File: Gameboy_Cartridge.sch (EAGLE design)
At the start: 8 parts

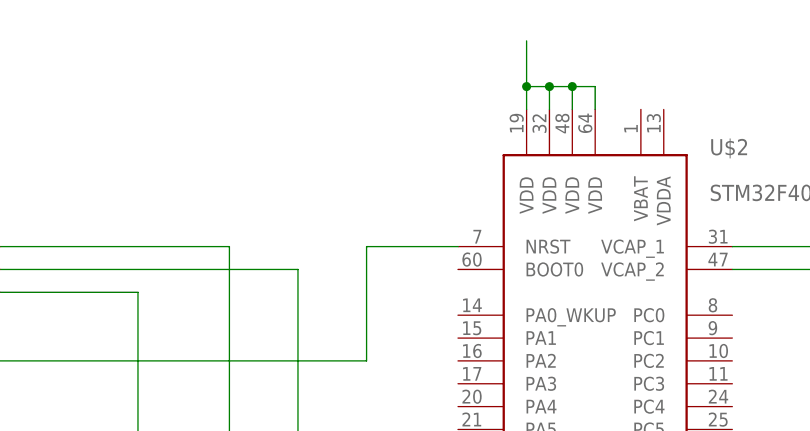
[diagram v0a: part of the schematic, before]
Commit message: BOOT0 10k pullup
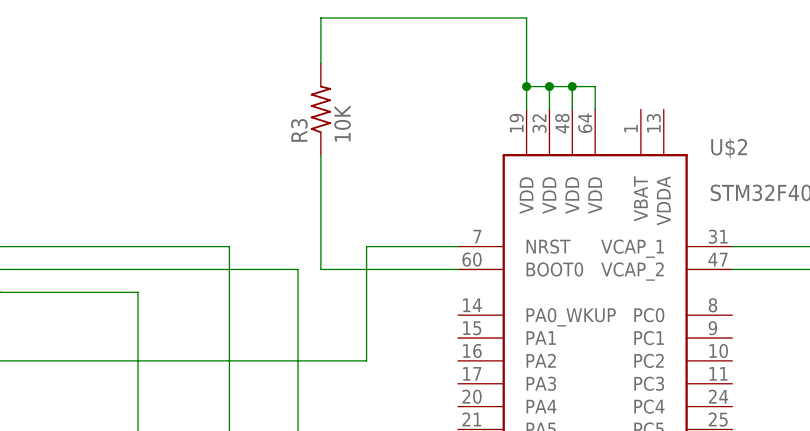
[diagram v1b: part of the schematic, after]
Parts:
- added R3: 10K, resistor:R-US_M0805
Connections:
- new net N$6: R3.1, U$2.BOOT0
- net N$1: now also R3.2
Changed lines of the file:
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@@
 <part name="C2" library="resistor" deviceset="C-EU" device="C0805" value="2.2uF"/>
 <part name="C3" library="resistor" deviceset="C-EU" device="C0805" value="2.2uF"/>
+<part name="R3" library="resistor" deviceset="R-US_" device="M0805" value="10K"/>
 </parts>
 <sheets>
@@
 <instance part="C2" gate="G$1" x="68.58" y="215.9" rot="R90"/>
 <instance part="C3" gate="G$1" x="78.74" y="213.36" rot="R90"/>
+<instance part="R3" gate="G$1" x="2.54" y="231.14" rot="R90"/>
 </instances>
 <busses>
@@
 <wire x1="27.94" y1="231.14" x2="27.94" y2="233.68" width="0.1524" layer="91"/>
 <junction x="27.94" y="233.68"/>
-<wire x1="25.4" y1="233.68" x2="25.4" y2="238.76" width="0.1524" layer="91"/>
+<wire x1="25.4" y1="233.68" x2="25.4" y2="241.3" width="0.1524" layer="91"/>
 <junction x="25.4" y="233.68"/>
+<pinref part="R3" gate="G$1" pin="2"/>
+<wire x1="2.54" y1="236.22" x2="2.54" y2="241.3" width="0.1524" layer="91"/>
+<wire x1="2.54" y1="241.3" x2="25.4" y2="241.3" width="0.1524" layer="91"/>
 </segment>
 </net>
@@
 </segment>
 </net>
+<net name="N$6" class="0">
+<segment>
+<pinref part="U$2" gate="G$1" pin="BOOT0"/>
+<wire x1="17.78" y1="213.36" x2="2.54" y2="213.36" width="0.1524" layer="91"/>
+<pinref part="R3" gate="G$1" pin="1"/>
+<wire x1="2.54" y1="213.36" x2="2.54" y2="226.06" width="0.1524" layer="91"/>
+</segment>
+</net>

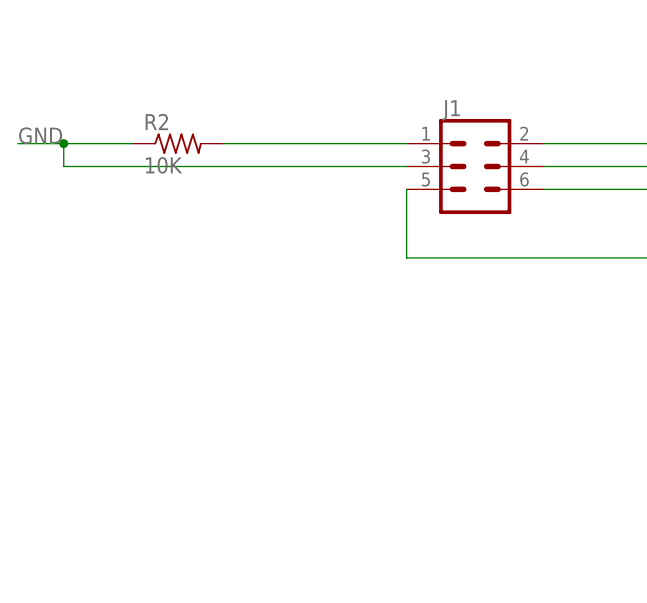
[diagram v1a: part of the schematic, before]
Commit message: add cap on NRST
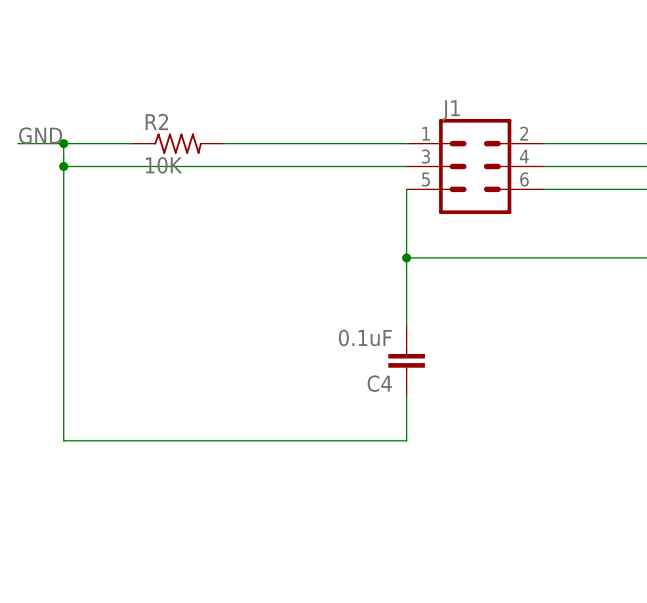
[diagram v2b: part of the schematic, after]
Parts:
- added C4: 0.1uF, resistor:C-EUC0805
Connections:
- net N$4: now also C4.1
- net N$8: now also C4.2
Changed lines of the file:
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@@
 <part name="C3" library="resistor" deviceset="C-EU" device="C0805" value="2.2uF"/>
 <part name="R3" library="resistor" deviceset="R-US_" device="M0805" value="10K"/>
+<part name="C4" library="resistor" deviceset="C-EU" device="C0805" value="0.1uF"/>
 </parts>
 <sheets>
@@
 <instance part="C3" gate="G$1" x="78.74" y="213.36" rot="R90"/>
 <instance part="R3" gate="G$1" x="2.54" y="231.14" rot="R90"/>
+<instance part="C4" gate="G$1" x="-48.26" y="190.5" rot="R180"/>
 </instances>
 <busses>
@@
 <wire x1="-86.36" y1="213.36" x2="-86.36" y2="215.9" width="0.1524" layer="91"/>
 <junction x="-86.36" y="215.9"/>
+<pinref part="C4" gate="G$1" pin="1"/>
+<wire x1="-48.26" y1="187.96" x2="-48.26" y2="182.88" width="0.1524" layer="91"/>
+<wire x1="-48.26" y1="182.88" x2="-86.36" y2="182.88" width="0.1524" layer="91"/>
+<wire x1="-86.36" y1="182.88" x2="-86.36" y2="213.36" width="0.1524" layer="91"/>
+<junction x="-86.36" y="213.36"/>
 </segment>
 </net>
@@
 <pinref part="U$2" gate="G$1" pin="NRST"/>
 <wire x1="7.62" y1="215.9" x2="17.78" y2="215.9" width="0.1524" layer="91"/>
+<pinref part="C4" gate="G$1" pin="2"/>
+<wire x1="-48.26" y1="195.58" x2="-48.26" y2="203.2" width="0.1524" layer="91"/>
+<junction x="-48.26" y="203.2"/>
 </segment>
 </net>
